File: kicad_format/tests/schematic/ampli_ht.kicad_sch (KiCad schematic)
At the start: 29 parts, among them P3 CONN_2, P4 CONN_2, Q1 MPSA92, Q2 MPSA42, Q3 MPSA92, Q4 MPSA42, U3 LM358N

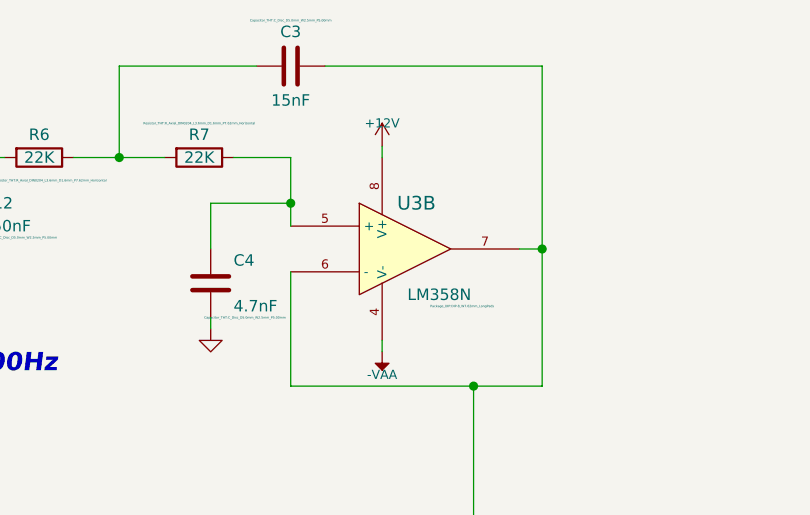
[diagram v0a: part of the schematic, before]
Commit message: Add serialization context and support most modern kicad file idiosyncrasies
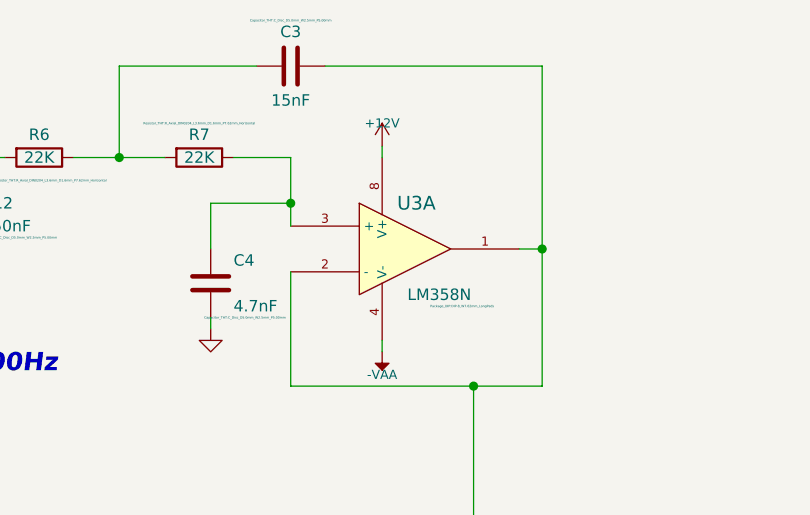
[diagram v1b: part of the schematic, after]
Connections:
- net Vpil_0_3,3V: now also U3.1, U3.2 (-); no longer U3.6 (-), U3.7
- net at C4.1, R7.1: now also U3.3 (+); no longer U3.5 (+)
